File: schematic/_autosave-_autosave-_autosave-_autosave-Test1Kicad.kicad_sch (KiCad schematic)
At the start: 75 parts, among them IC1 BMI055, J1 Power Module 1, J10 CAP & ADC IN, J11 SPI Port, J12 I2C A, J13 FMU PWM OUT, J14 PPM RC, J15 2908-05WB-MG, J16 RC, J17 SBUS, J18 IO/PWM out, J2 Power Module 2, J3 USB, J4 Telemetry 1, J5 Telemetry 2, J6 UART & I2C B, J7 CAN 1, J8 CAN 2, J9 GPS Module, U1 STM32F765IIKx, U10 TJA1051TK-3, U11 LT3080xDD, U12 LP5907MFX-3.3, U3 IST8310, U4 ICM-20602, U5 ICM-20689, U6 MS5611-01BA, U8 STM32F103V8Tx, U9 TJA1051TK-3, Y1 ABM2-8.000MHZ-D4Y-T

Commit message: renamed vdd sensors and ports to reg_3v
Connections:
- net REG_3V: no longer U1.C7 (VDD), U1.C9 (VDD)
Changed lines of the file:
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@@
 	)
 	(junction
-		(at 123.19 17.78)
-		(diameter 0)
-		(color 0 0 0 0)
-	)
-	(junction
 		(at 525.78 38.1)
 		(diameter 0)
@@
 	(wire
 		(pts
-			(xy 123.19 17.78) (xy 127 17.78)
-		)
-		(stroke
-			(width 0)
-			(type default)
-		)
-	)
-	(wire
-		(pts
 			(xy 259.08 78.74) (xy 259.08 73.66)
 		)
@@
 	(wire
 		(pts
-			(xy 118.11 17.78) (xy 123.19 17.78)
-		)
-		(stroke
-			(width 0)
-			(type default)
-		)
-	)
-	(wire
-		(pts
 			(xy 334.01 165.1) (xy 345.44 165.1)
 		)
@@
 	(wire
 		(pts
-			(xy 123.19 20.32) (xy 123.19 17.78)
-		)
-		(stroke
-			(width 0)
-			(type default)
-		)
-	)
-	(wire
-		(pts
 			(xy 356.87 270.51) (xy 356.87 276.86)
 		)
@@
 	(wire
 		(pts
-			(xy 127 20.32) (xy 123.19 20.32)
-		)
-		(stroke
-			(width 0)
-			(type default)
-		)
-	)
-	(wire
-		(pts
 			(xy 292.1 120.65) (xy 294.64 120.65)
 		)
@@
 		)
 	)
-	(global_label "VDD_ports"
-		(shape input)
-		(at 154.94 26.67 90)
-		(fields_autoplaced yes)
-		(effects
-			(font
-				(size 1.27 1.27)
-			)
-			(justify left)
-		)
-		(property "Intersheetrefs" "${INTERSHEET_REFS}"
-			(at 154.94 14.2506 90)
-			(effects
-				(font
-					(size 1.27 1.27)
-				)
-				(justify left)
-				(hide yes)
-			)
-		)
-	)
 	(global_label "FMU_CH1"
 		(shape input)
@@
 		)
 	)
-	(global_label "VDDIO_sensors"
+	(global_label "REG_3V"
 		(shape input)
 		(at 318.77 153.67 180)
@@
 		)
 		(property "Intersheetrefs" "${INTERSHEET_REFS}"
-			(at 301.9962 153.67 0)
+			(at 308.8301 153.67 0)
 			(effects
 				(font
@@
 		)
 	)
-	(global_label "VDDIO_sensors"
+	(global_label "REG_3V"
 		(shape input)
 		(at 281.94 92.71 0)
@@
 		)
 		(property "Intersheetrefs" "${INTERSHEET_REFS}"
-			(at 298.7138 92.71 0)
+			(at 291.8799 92.71 0)
 			(effects
 				(font
@@
 		)
 	)
-	(global_label "REG_3V"
-		(shape input)
-		(at 118.11 17.78 180)
-		(fields_autoplaced yes)
-		(effects
-			(font
-				(size 1.27 1.27)
-			)
-			(justify right)
-		)
-		(property "Intersheetrefs" "${INTERSHEET_REFS}"
-			(at 108.1701 17.78 0)
-			(effects
-				(font
-					(size 1.27 1.27)
-				)
-				(justify right)
-				(hide yes)
-			)
-		)
-	)
 	(global_label "CAN1_RX"
 		(shape input)
@@
 		)
 	)
-	(global_label "VDDIO_sensors"
+	(global_label "REG_3V"
 		(shape input)
 		(at 345.44 165.1 0)
@@
 		)
 		(property "Intersheetrefs" "${INTERSHEET_REFS}"
-			(at 362.2138 165.1 0)
+			(at 355.3799 165.1 0)
 			(effects
 				(font
@@
 		)
 	)
-	(global_label "VDD_ports"
+	(global_label "REG_3V"
 		(shape input)
 		(at 445.77 251.46 180)
@@
 		)
 		(property "Intersheetrefs" "${INTERSHEET_REFS}"
-			(at 433.3506 251.46 0)
+			(at 435.8301 251.46 0)
 			(effects
 				(font
@@
 		)
 	)
-	(global_label "VDDIO_sensors"
-		(shape input)
-		(at 127 17.78 0)
-		(fields_autoplaced yes)
-		(effects
-			(font
-				(size 1.27 1.27)
-			)
-			(justify left)
-		)
-		(property "Intersheetrefs" "${INTERSHEET_REFS}"
-			(at 143.7738 17.78 0)
-			(effects
-				(font
-					(size 1.27 1.27)
-				)
-				(justify left)
-				(hide yes)
-			)
-		)
-	)
 	(global_label "FMU_CH5"
 		(shape input)
@@
 		)
 	)
-	(global_label "VDD_ports"
-		(shape input)
-		(at 127 20.32 0)
-		(fields_autoplaced yes)
-		(effects
-			(font
-				(size 1.27 1.27)
-			)
-			(justify left)
-		)
-		(property "Intersheetrefs" "${INTERSHEET_REFS}"
-			(at 139.4194 20.32 0)
-			(effects
-				(font
-					(size 1.27 1.27)
-				)
-				(justify left)
-				(hide yes)
-			)
-		)
-	)
 	(global_label "IO_CH6"
 		(shape input)
@@
 		)
 	)
-	(global_label "VDDIO_sensors"
-		(shape input)
-		(at 152.4 26.67 90)
-		(fields_autoplaced yes)
-		(effects
-			(font
-				(size 1.27 1.27)
-			)
-			(justify left)
-		)
-		(property "Intersheetrefs" "${INTERSHEET_REFS}"
-			(at 152.4 9.8962 90)
-			(effects
-				(font
-					(size 1.27 1.27)
-				)
-				(justify left)
-				(hide yes)
-			)
-		)
-	)
 	(global_label "nSAFETY_SWITCH_LED_OUT"
 		(shape input)
@@
 		)
 	)
-	(global_label "VDD_ports"
+	(global_label "REG_3V"
 		(shape input)
 		(at 458.47 321.31 0)
@@
 		)
 		(property "Intersheetrefs" "${INTERSHEET_REFS}"
-			(at 470.8894 321.31 0)
+			(at 468.4099 321.31 0)
 			(effects
 				(font

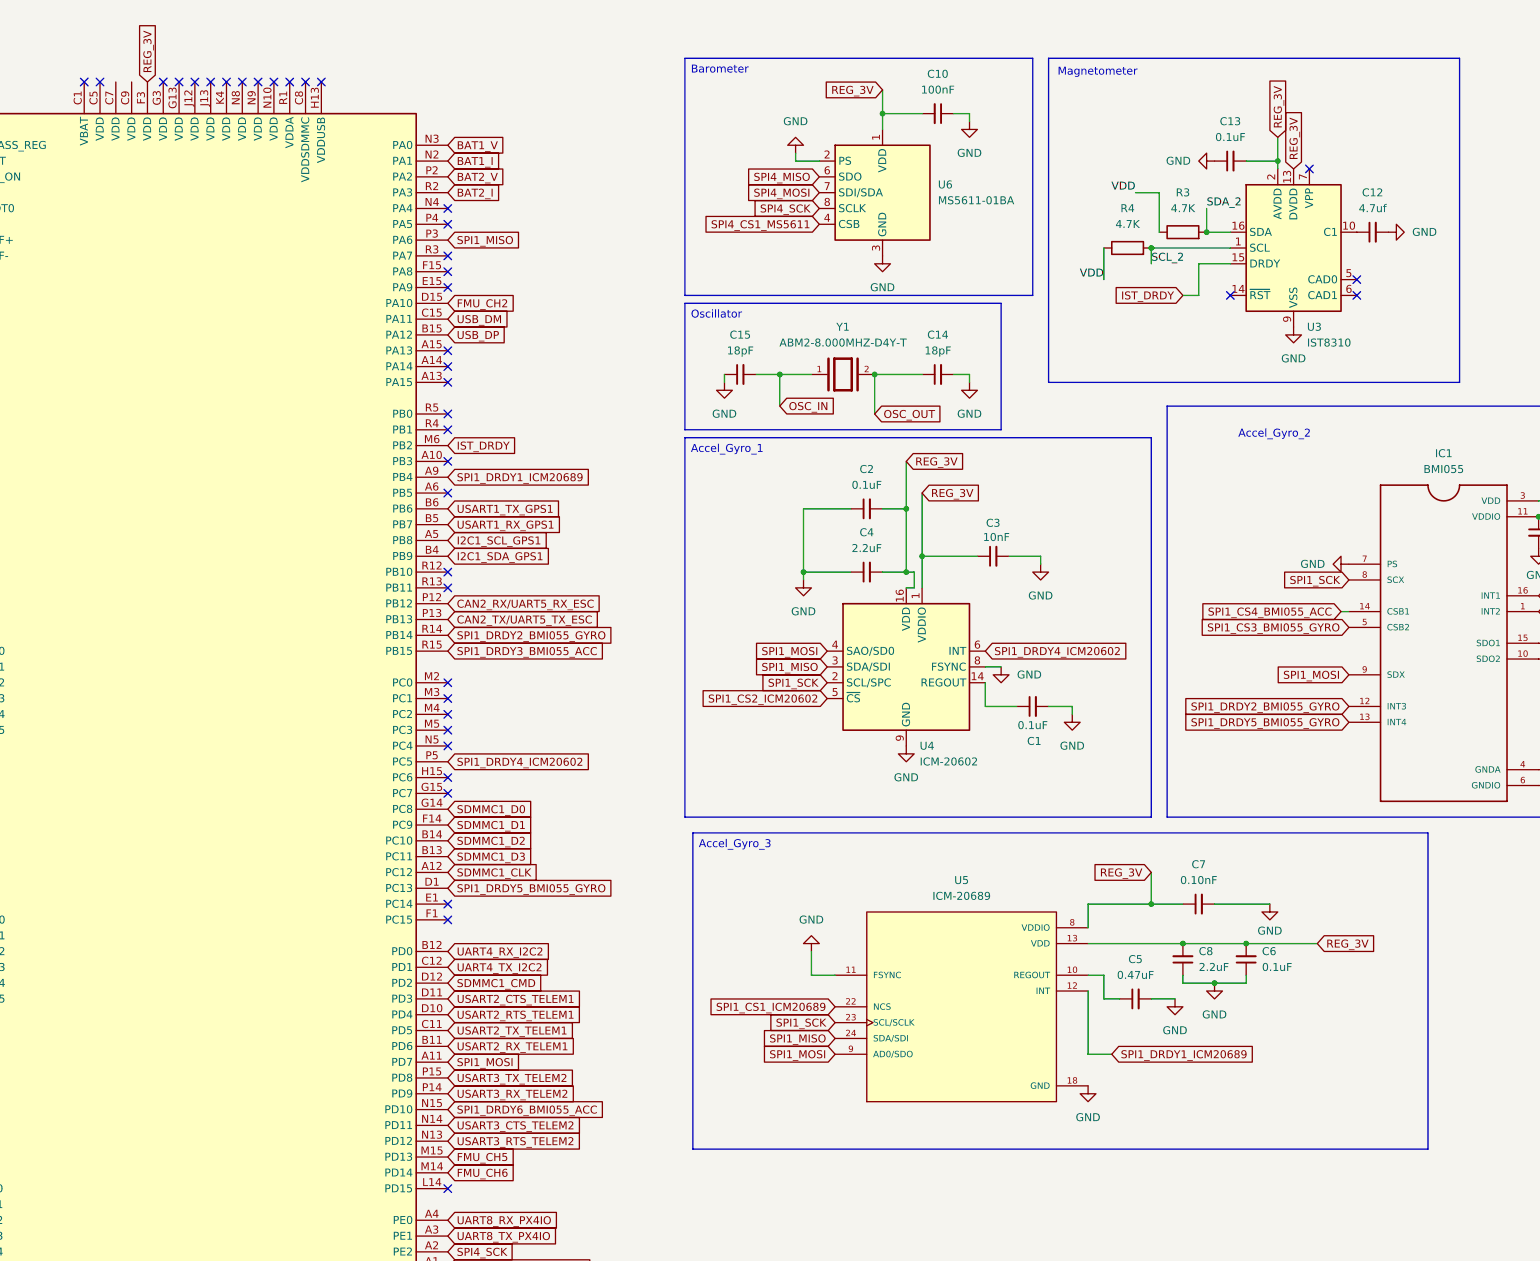
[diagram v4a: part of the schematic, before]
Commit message: redid ICM-20689 with new symbol
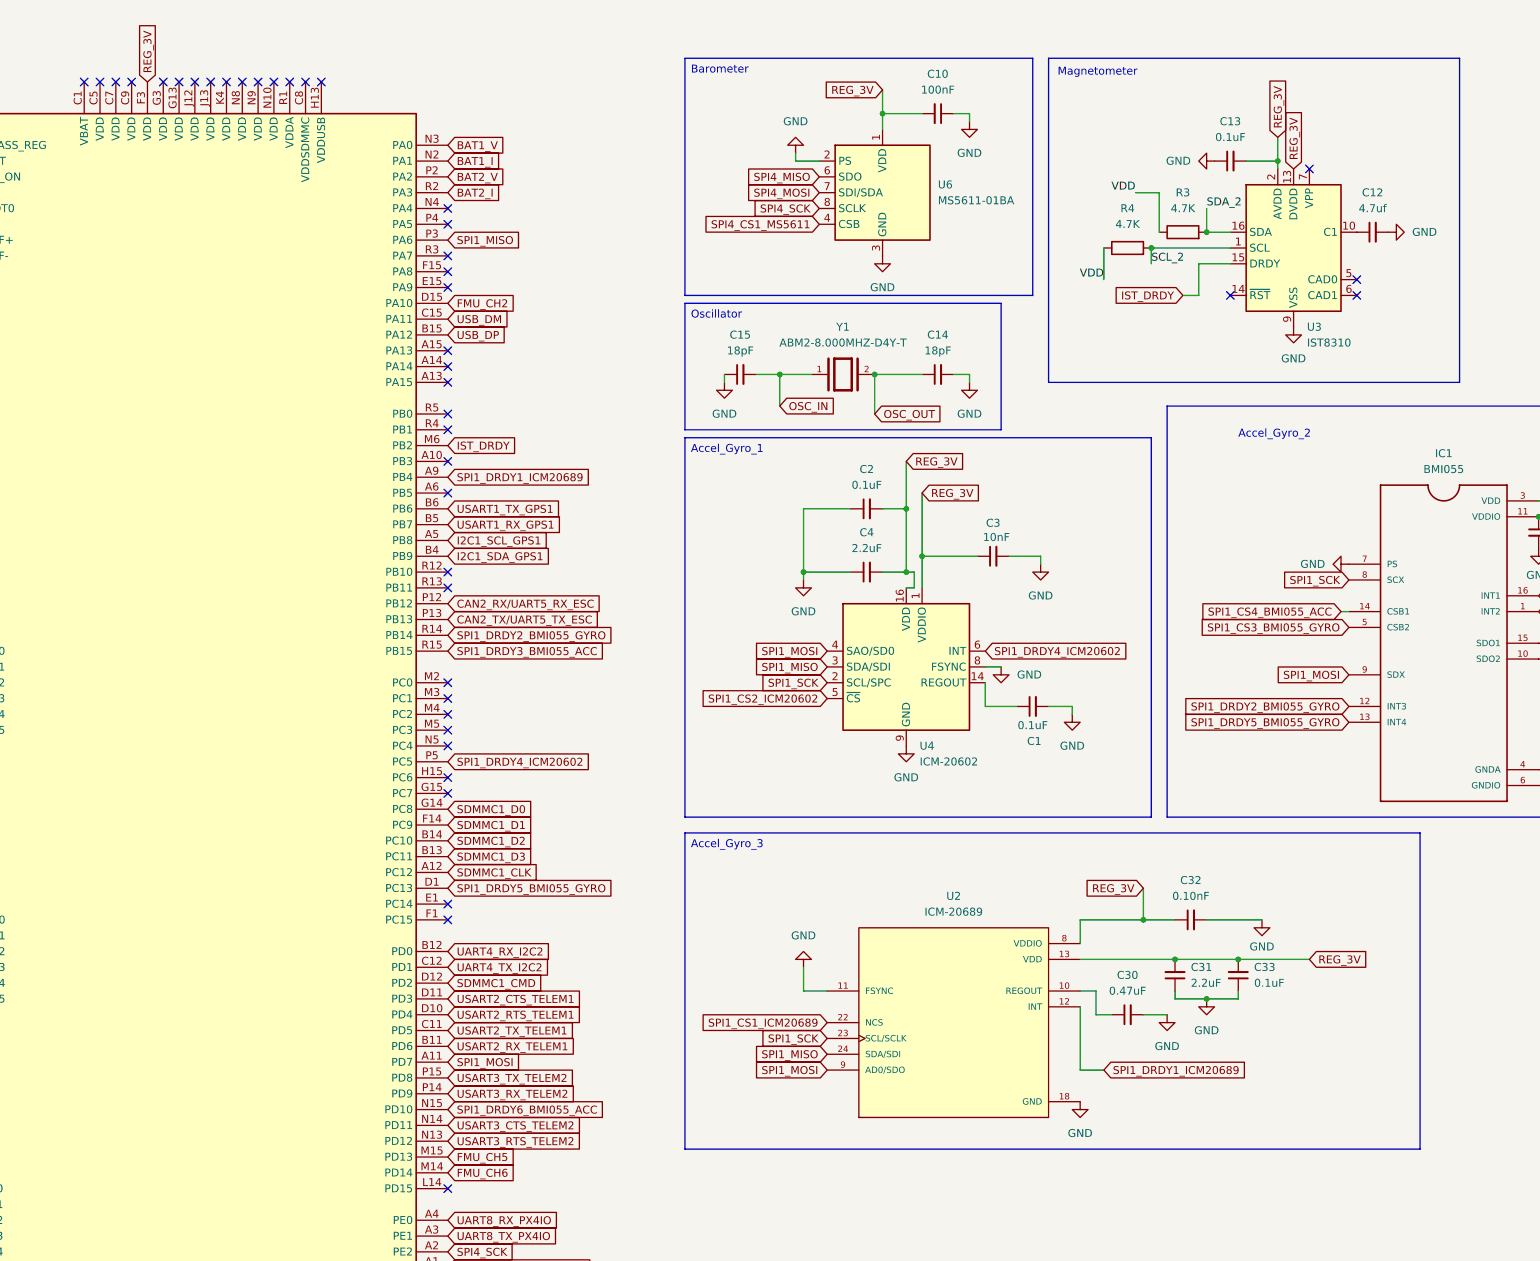
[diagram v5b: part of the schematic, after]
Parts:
- removed C5: 0.47uF, Capacitor_SMD:C_0603_1608Metric, symbol Device:C_Small
- removed C6: 0.1uF, Capacitor_SMD:C_0603_1608Metric, symbol Device:C_Small
- removed C7: 0.10nF, Capacitor_SMD:C_0603_1608Metric, symbol Device:C_Small
- removed C8: 2.2uF, Capacitor_SMD:C_0603_1608Metric, symbol Device:C_Small
- removed U5: ICM-20689, Sensor_Motion:InvenSense_QFN-24_4x4mm_P0.5mm, symbol ICM-20689:ICM-20689
- added C30: 0.47uF, Capacitor_SMD:C_0603_1608Metric, symbol Device:C_Small
- added C31: 2.2uF, Capacitor_SMD:C_0603_1608Metric, symbol Device:C_Small
- added C32: 0.10nF, Capacitor_SMD:C_0603_1608Metric, symbol Device:C_Small
- added C33: 0.1uF, Capacitor_SMD:C_0603_1608Metric, symbol Device:C_Small
- added U2: ICM-20689, ICM-20689:QFN50P400X400X95-24N, symbol ICM-20689:ICM-20689
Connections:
- net GND: now also C30.2, C31.1, C32.2, C33.1, U2.11 (FSYNC), U2.18 (GND)
- net REG_3V: now also C31.2, C32.1, C33.2, U2.13 (VDD), U2.8 (VDDIO)
- net SPI1_CS1_ICM20689: now also U2.22 (NCS)
- net SPI1_DRDY1_ICM20689: now also U2.12 (INT)
- net SPI1_MISO: now also U2.24 (SDA/SDI)
- net SPI1_MOSI: now also U2.9 (AD0/SDO)
- net SPI1_SCK: now also U2.23 (SCL/SCLK)
- new net: C30.1, U2.10 (REGOUT)
- no-connect marks 156 -> 158

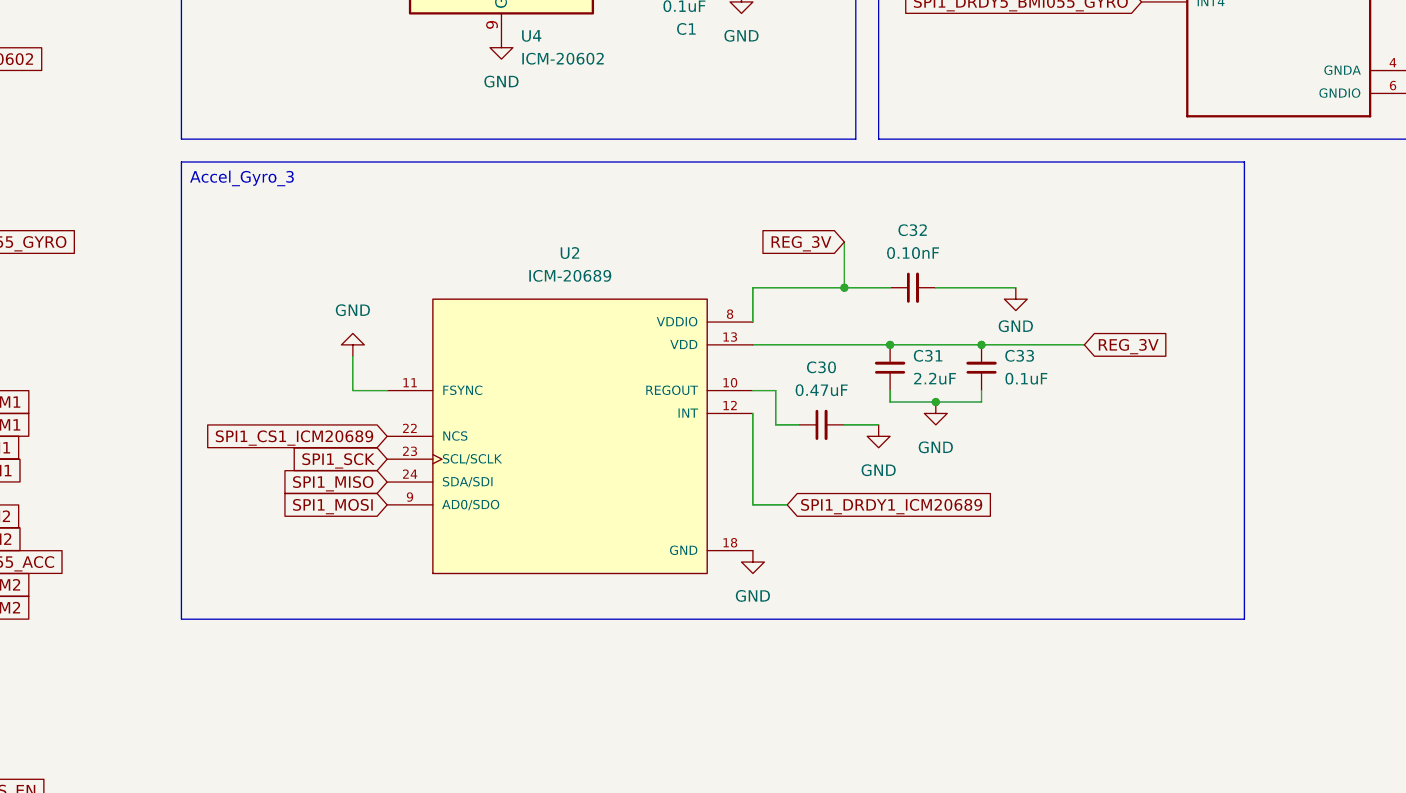
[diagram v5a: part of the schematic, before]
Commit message: replaced ICM20689 symbol
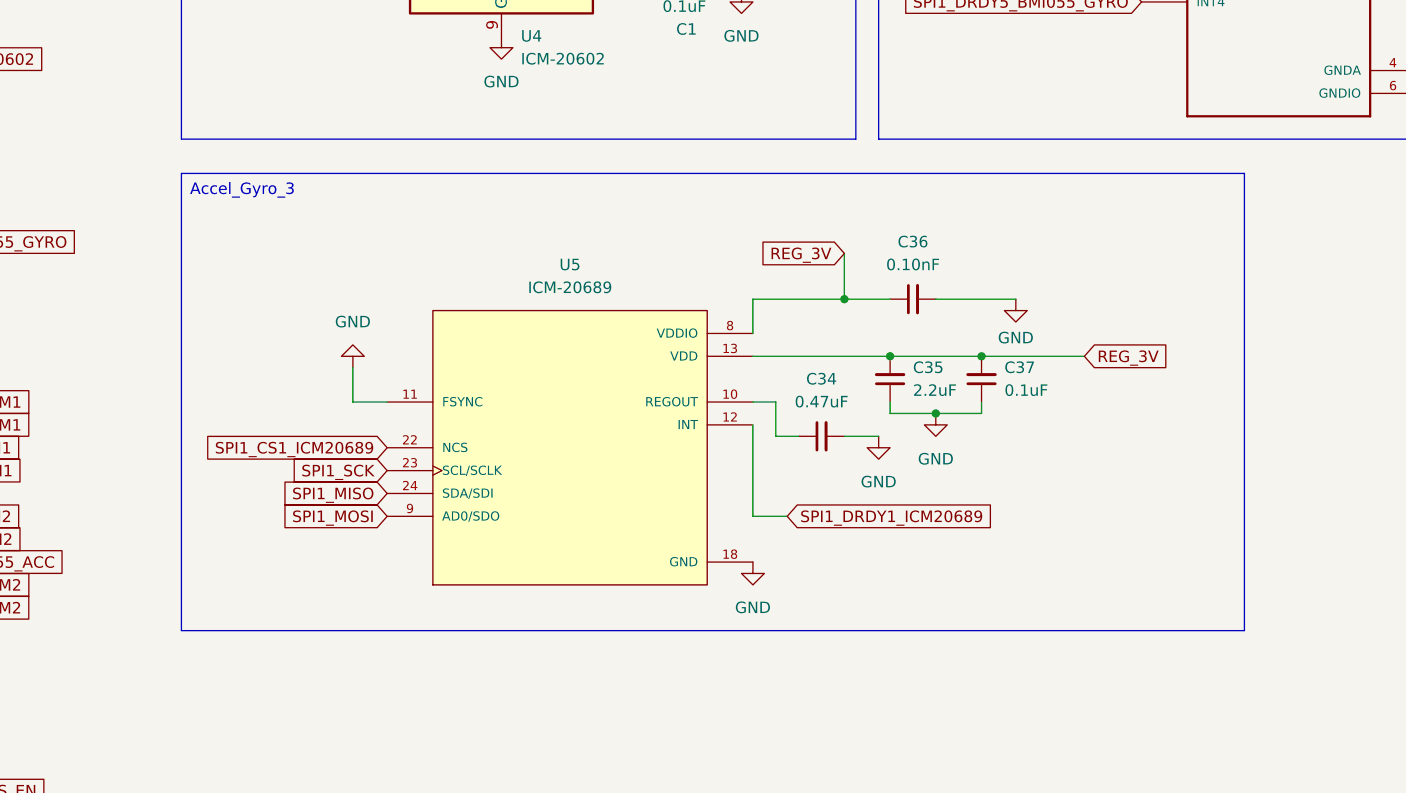
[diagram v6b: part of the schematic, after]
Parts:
- removed C30: 0.47uF, Capacitor_SMD:C_0603_1608Metric, symbol Device:C_Small
- removed C31: 2.2uF, Capacitor_SMD:C_0603_1608Metric, symbol Device:C_Small
- removed C32: 0.10nF, Capacitor_SMD:C_0603_1608Metric, symbol Device:C_Small
- removed C33: 0.1uF, Capacitor_SMD:C_0603_1608Metric, symbol Device:C_Small
- removed U2: ICM-20689, ICM-20689:QFN50P400X400X95-24N, symbol ICM-20689:ICM-20689
- added C34: 0.47uF, Capacitor_SMD:C_0603_1608Metric, symbol Device:C_Small
- added C35: 2.2uF, Capacitor_SMD:C_0603_1608Metric, symbol Device:C_Small
- added C36: 0.10nF, Capacitor_SMD:C_0603_1608Metric, symbol Device:C_Small
- added C37: 0.1uF, Capacitor_SMD:C_0603_1608Metric, symbol Device:C_Small
- added U5: ICM-20689, ICM-20689:QFN50P400X400X95-24N, symbol ICM-20689:ICM-20689
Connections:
- net GND: now also C34.2, C35.1, C36.2, C37.1, U5.11 (FSYNC), U5.18 (GND)
- net REG_3V: now also C35.2, C36.1, C37.2, U5.13 (VDD), U5.8 (VDDIO)
- net SPI1_CS1_ICM20689: now also U5.22 (NCS)
- net SPI1_DRDY1_ICM20689: now also U5.12 (INT)
- net SPI1_MISO: now also U5.24 (SDA/SDI)
- net SPI1_MOSI: now also U5.9 (AD0/SDO)
- net SPI1_SCK: now also U5.23 (SCL/SCLK)
- new net: C34.1, U5.10 (REGOUT)
